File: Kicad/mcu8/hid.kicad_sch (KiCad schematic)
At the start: 27 parts, among them IC401 MCP2221A, K401 FRONT #1, K402 FRONT #2, K403 VIN, K404 +5V, K405 FRONT #3, K406 SERVO LEFT, K407 USB/UART, K408 SERVO RIGHT

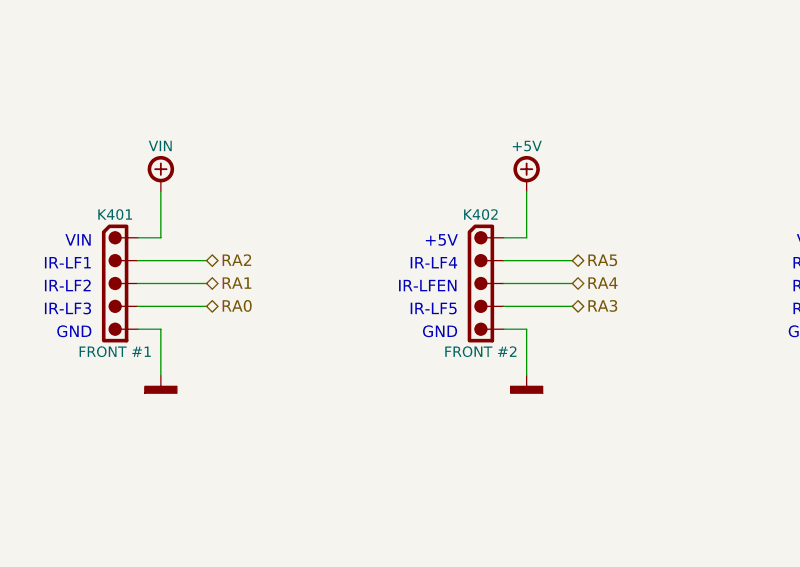
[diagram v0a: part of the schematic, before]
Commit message: Update MCU 8Bit
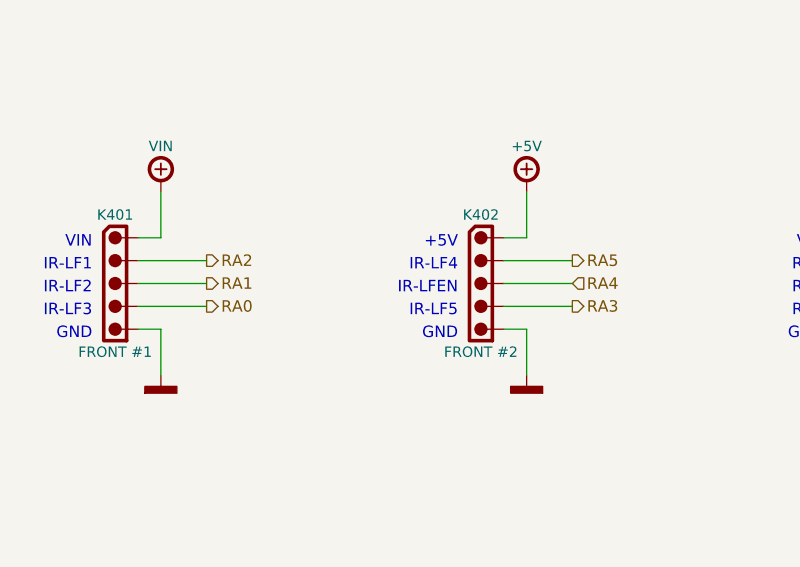
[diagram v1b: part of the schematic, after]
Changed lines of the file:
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@@
     (effects (font (size 1.27 1.27)) (justify left bottom))
   )
-  (hierarchical_label "RA2" (shape bidirectional) (at 66.04 58.42 0)
+  (hierarchical_label "RA2" (shape output) (at 66.04 58.42 0)
     (effects (font (size 1.27 1.27)) (justify left))
   )
-  (hierarchical_label "RA0" (shape bidirectional) (at 66.04 63.5 0)
+  (hierarchical_label "RA0" (shape output) (at 66.04 63.5 0)
     (effects (font (size 1.27 1.27)) (justify left))
   )
@@
     (effects (font (size 1.27 1.27)) (justify left))
   )
-  (hierarchical_label "RA1" (shape bidirectional) (at 66.04 60.96 0)
+  (hierarchical_label "RA1" (shape output) (at 66.04 60.96 0)
     (effects (font (size 1.27 1.27)) (justify left))
   )
@@
     (effects (font (size 1.27 1.27)) (justify right))
   )
-  (hierarchical_label "RA5" (shape bidirectional) (at 106.68 58.42 0)
+  (hierarchical_label "RA5" (shape output) (at 106.68 58.42 0)
     (effects (font (size 1.27 1.27)) (justify left))
   )
@@
     (effects (font (size 1.27 1.27)) (justify right))
   )
-  (hierarchical_label "RA4" (shape bidirectional) (at 106.68 60.96 0)
+  (hierarchical_label "RA4" (shape input) (at 106.68 60.96 0)
     (effects (font (size 1.27 1.27)) (justify left))
   )
@@
     (effects (font (size 1.27 1.27)) (justify left))
   )
-  (hierarchical_label "RA3" (shape bidirectional) (at 106.68 63.5 0)
+  (hierarchical_label "RA3" (shape output) (at 106.68 63.5 0)
     (effects (font (size 1.27 1.27)) (justify left))
   )

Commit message: Update MCU 8Bit
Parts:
- renumbered BB401 to BB301, C401 to C301, C402 to C302, C403 to C303, C404 to C304, IC401 to IC301, K401 to K301, K402 to K302, K403 to K303, K404 to K304, K405 to K305, K406 to K306, K407 to K307, K408 to K308, LED401 to LED301, LED402 to LED302, LED403 to LED303, R401 to R301, R402 to R302, R403 to R303, R404 to R304, R405 to R305, R406 to R306, R407 to R307, R408 to R308, R409 to R309, S401 to S301
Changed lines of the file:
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@@
   (symbol (lib_id "tronixio:R-1206") (at 80.01 165.1 270) (unit 1)
     (in_bom yes) (on_board yes)
-    (property "Reference" "R403" (id 0) (at 80.01 162.56 90)
+    (property "Reference" "R303" (id 0) (at 80.01 162.56 90)
       (effects (font (size 1.15 1.15)))
     )
@@
   (symbol (lib_id "tronixio:FCI-USB-TYPE-B-MICRO-THT") (at 182.88 60.96 0) (unit 1)
     (in_bom yes) (on_board yes)
-    (property "Reference" "K407" (id 0) (at 182.88 48.26 0)
+    (property "Reference" "K307" (id 0) (at 182.88 48.26 0)
       (effects (font (size 1.15 1.15)))
     )
@@
   (symbol (lib_id "tronixio:MOLEX-MICRO-LATCH-05-VERTICAL") (at 55.88 55.88 0) (mirror y) (unit 1)
     (in_bom yes) (on_board yes)
-    (property "Reference" "K401" (id 0) (at 55.88 53.34 0)
+    (property "Reference" "K301" (id 0) (at 55.88 53.34 0)
       (effects (font (size 1.15 1.15)))
     )
@@
   (symbol (lib_id "tronixio:UVZ-220U-25V") (at 172.72 127 0) (unit 1)
     (in_bom yes) (on_board yes)
-    (property "Reference" "C401" (id 0) (at 173.355 124.46 0)
+    (property "Reference" "C301" (id 0) (at 173.355 124.46 0)
       (effects (font (size 1.15 1.15)) (justify left))
     )
@@
   (symbol (lib_id "tronixio:MOLEX-MICRO-LATCH-05-VERTICAL") (at 137.16 55.88 0) (mirror y) (unit 1)
     (in_bom yes) (on_board yes)
-    (property "Reference" "K405" (id 0) (at 137.16 53.34 0)
+    (property "Reference" "K305" (id 0) (at 137.16 53.34 0)
       (effects (font (size 1.15 1.15)))
     )
@@
   (symbol (lib_id "tronixio:R-1206") (at 241.3 119.38 270) (unit 1)
     (in_bom yes) (on_board yes)
-    (property "Reference" "R408" (id 0) (at 241.3 116.84 90)
+    (property "Reference" "R308" (id 0) (at 241.3 116.84 90)
       (effects (font (size 1.15 1.15)))
     )
@@
   (symbol (lib_id "tronixio:E-SWITCH-TL1240RQ1JCLR") (at 88.9 170.18 270) (mirror x) (unit 1)
     (in_bom yes) (on_board yes)
-    (property "Reference" "S401" (id 0) (at 92.71 173.99 90)
+    (property "Reference" "S301" (id 0) (at 92.71 173.99 90)
       (effects (font (size 1.15 1.15)))
     )
@@
   (symbol (lib_id "tronixio:HARWIN-254-F-1X08-VERTICAL") (at 129.54 109.22 0) (mirror y) (unit 1)
     (in_bom yes) (on_board yes)
-    (property "Reference" "K404" (id 0) (at 129.54 106.68 0)
+    (property "Reference" "K304" (id 0) (at 129.54 106.68 0)
       (effects (font (size 1.15 1.15)))
     )
@@
   (symbol (lib_id "tronixio:R-1206") (at 238.76 60.96 180) (unit 1)
     (in_bom yes) (on_board yes)
-    (property "Reference" "R407" (id 0) (at 241.3 57.15 0)
+    (property "Reference" "R307" (id 0) (at 241.3 57.15 0)
       (effects (font (size 1.15 1.15)))
     )
@@
   (symbol (lib_id "tronixio:R-1206") (at 180.34 119.38 270) (unit 1)
     (in_bom yes) (on_board yes)
-    (property "Reference" "R405" (id 0) (at 180.34 116.84 90)
+    (property "Reference" "R305" (id 0) (at 180.34 116.84 90)
       (effects (font (size 1.15 1.15)))
     )
@@
   (symbol (lib_id "tronixio:LED-1206-PURPLE") (at 238.76 40.64 270) (mirror x) (unit 1)
     (in_bom yes) (on_board yes)
-    (property "Reference" "LED402" (id 0) (at 240.03 35.56 0)
+    (property "Reference" "LED302" (id 0) (at 240.03 35.56 0)
       (effects (font (size 1.15 1.15)))
     )
@@
   (symbol (lib_id "tronixio:R-1206") (at 80.01 154.94 270) (unit 1)
     (in_bom yes) (on_board yes)
-    (property "Reference" "R402" (id 0) (at 80.01 152.4 90)
+    (property "Reference" "R302" (id 0) (at 80.01 152.4 90)
       (effects (font (size 1.15 1.15)))
     )
@@
   (symbol (lib_id "tronixio:UVZ-220U-25V") (at 233.68 127 0) (unit 1)
     (in_bom yes) (on_board yes)
-    (property "Reference" "C404" (id 0) (at 234.315 124.46 0)
+    (property "Reference" "C304" (id 0) (at 234.315 124.46 0)
       (effects (font (size 1.15 1.15)) (justify left))
     )
@@
   (symbol (lib_id "tronixio:HARWIN-254-M-1X04-VERTICAL") (at 162.56 114.3 0) (mirror y) (unit 1)
     (in_bom yes) (on_board yes)
-    (property "Reference" "K406" (id 0) (at 162.56 111.76 0)
+    (property "Reference" "K306" (id 0) (at 162.56 111.76 0)
       (effects (font (size 1.15 1.15)))
     )
@@
   (symbol (lib_id "tronixio:HARWIN-254-F-1X08-VERTICAL") (at 96.52 109.22 0) (mirror y) (unit 1)
     (in_bom yes) (on_board yes)
-    (property "Reference" "K403" (id 0) (at 96.52 106.68 0)
+    (property "Reference" "K303" (id 0) (at 96.52 106.68 0)
       (effects (font (size 1.15 1.15)))
     )
@@
   (symbol (lib_id "tronixio:R-1206") (at 243.84 60.96 180) (unit 1)
     (in_bom yes) (on_board yes)
-    (property "Reference" "R409" (id 0) (at 246.38 57.15 0)
+    (property "Reference" "R309" (id 0) (at 246.38 57.15 0)
       (effects (font (size 1.15 1.15)))
     )
@@
   (symbol (lib_id "tronixio:BREADBOARD-170") (at 59.69 116.84 0) (unit 1)
     (in_bom yes) (on_board yes)
-    (property "Reference" "BB401" (id 0) (at 59.69 107.95 0)
+    (property "Reference" "BB301" (id 0) (at 59.69 107.95 0)
       (effects (font (size 1.15 1.15)))
     )
@@
   (symbol (lib_id "tronixio:R-1206") (at 73.66 149.86 180) (unit 1)
     (in_bom yes) (on_board yes)
-    (property "Reference" "R401" (id 0) (at 68.58 146.05 0)
+    (property "Reference" "R301" (id 0) (at 68.58 146.05 0)
       (effects (font (size 1.15 1.15)) (justify right))
     )
@@
   (symbol (lib_id "tronixio:C-1206") (at 200.66 73.66 0) (unit 1)
     (in_bom yes) (on_board yes)
-    (property "Reference" "C402" (id 0) (at 200.66 71.12 0)
+    (property "Reference" "C302" (id 0) (at 200.66 71.12 0)
       (effects (font (size 1.15 1.15)) (justify right))
     )
@@
   (symbol (lib_id "tronixio:R-1206") (at 200.66 40.64 180) (unit 1)
     (in_bom yes) (on_board yes)
-    (property "Reference" "R406" (id 0) (at 200.66 36.83 0)
+    (property "Reference" "R306" (id 0) (at 200.66 36.83 0)
       (effects (font (size 1.15 1.15)) (justify left))
     )
@@
   (symbol (lib_id "tronixio:LED-1206-PURPLE") (at 134.62 172.72 270) (mirror x) (unit 1)
     (in_bom yes) (on_board yes)
-    (property "Reference" "LED401" (id 0) (at 135.255 169.545 90)
+    (property "Reference" "LED301" (id 0) (at 135.255 169.545 90)
       (effects (font (size 1.15 1.15)) (justify left))
     )
@@
   (symbol (lib_id "tronixio:HARWIN-254-M-1X04-VERTICAL") (at 223.52 114.3 0) (mirror y) (unit 1)
     (in_bom yes) (on_board yes)
-    (property "Reference" "K408" (id 0) (at 223.52 111.76 0)
+    (property "Reference" "K308" (id 0) (at 223.52 111.76 0)
       (effects (font (size 1.15 1.15)))
     )
@@
   (symbol (lib_id "tronixio:R-1206") (at 134.62 165.1 180) (unit 1)
     (in_bom yes) (on_board yes)
-    (property "Reference" "R404" (id 0) (at 139.7 161.29 0)
+    (property "Reference" "R304" (id 0) (at 139.7 161.29 0)
       (effects (font (size 1.15 1.15)) (justify left))
     )
@@
   (symbol (lib_id "tronixio:MCP2221A-ISL") (at 223.52 58.42 0) (unit 1)
     (in_bom yes) (on_board yes)
-    (property "Reference" "IC401" (id 0) (at 215.9 44.45 0)
+    (property "Reference" "IC301" (id 0) (at 215.9 44.45 0)
       (effects (font (size 1.15 1.15)) (justify left))
     )
@@
   (symbol (lib_id "tronixio:MOLEX-MICRO-LATCH-05-VERTICAL") (at 96.52 55.88 0) (mirror y) (unit 1)
     (in_bom yes) (on_board yes)
-    (property "Reference" "K402" (id 0) (at 96.52 53.34 0)
+    (property "Reference" "K302" (id 0) (at 96.52 53.34 0)
       (effects (font (size 1.15 1.15)))
     )
@@
   (symbol (lib_id "tronixio:E-SWITCH-TL1240RQ1JCLR") (at 73.66 160.02 90) (unit 2)
     (in_bom yes) (on_board yes)
-    (property "Reference" "S401" (id 0) (at 67.31 156.845 90)
+    (property "Reference" "S301" (id 0) (at 67.31 156.845 90)
       (effects (font (size 1.15 1.15)) (justify right))
     )
@@
   (symbol (lib_id "tronixio:C-1206") (at 205.74 73.66 0) (unit 1)
     (in_bom yes) (on_board yes)
-    (property "Reference" "C403" (id 0) (at 205.74 71.12 0)
+    (property "Reference" "C303" (id 0) (at 205.74 71.12 0)
       (effects (font (size 1.15 1.15)) (justify right))
     )
@@
   (symbol (lib_id "tronixio:LED-1206-PURPLE") (at 243.84 40.64 270) (mirror x) (unit 1)
     (in_bom yes) (on_board yes)
-    (property "Reference" "LED403" (id 0) (at 245.11 35.56 0)
-      (effects (font (size 1.15 1.15)))
-    )
+    (property "Reference" "LED303" (id 0) (at 245.11 35.56 0)
+      (effects (font (size 1.15 1.15)))
+    )

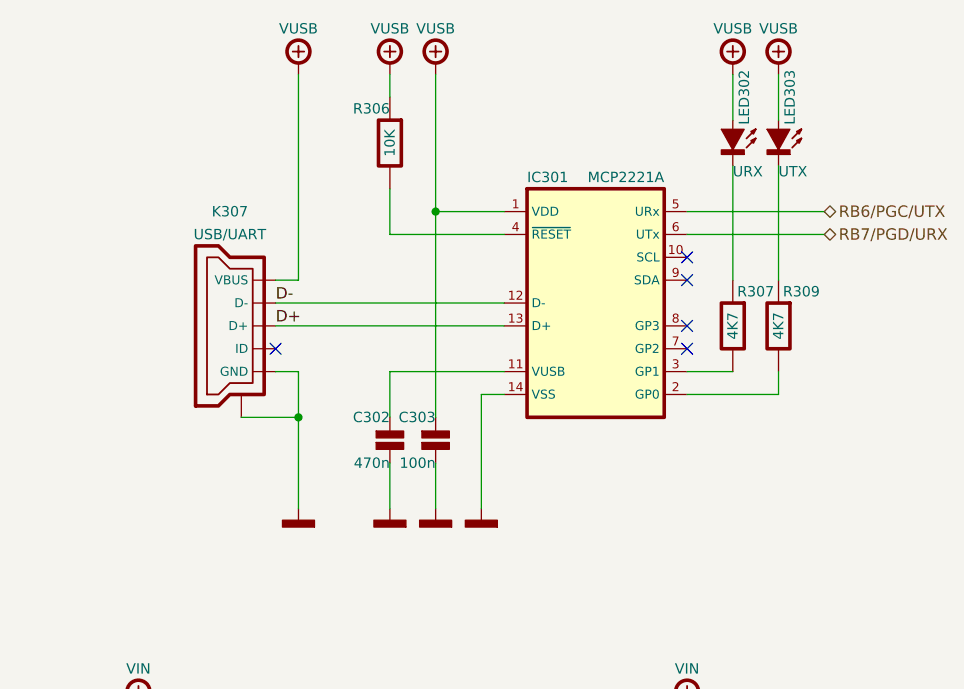
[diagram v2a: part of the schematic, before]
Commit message: Update hid.kicad_sch
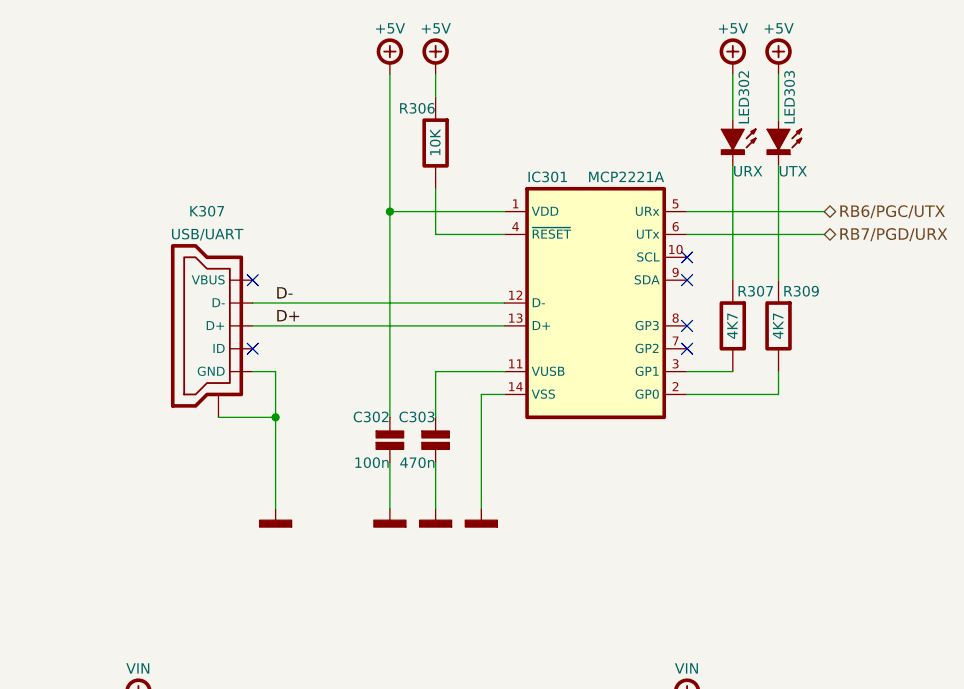
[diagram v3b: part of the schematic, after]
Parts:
- renumbered C303 to C302, C302 to C303
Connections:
- net +5V: now also C302.1, IC301.1 (VDD), LED302.2 (A), LED303.2 (A), R306.2
- removed net VUSB: C302.1, IC301.1 (VDD), K307.1 (VBUS), LED302.2 (A), LED303.2 (A), R306.2
- no-connect marks 5 -> 6
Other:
- moved on the sheet: C302, C303, K307, R306
